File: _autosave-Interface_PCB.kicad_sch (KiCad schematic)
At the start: 40 parts, among them IC1 STM32L412RBT6P, J1 USB_B, J2 AVR-JTAG-10, J3 Conn_01x04, J4 Conn_01x04, J5 Conn_01x04, J6 Conn_01x04, J7 Micro_SD_Card, U1 AMS1117-3.3, Y1 Crystal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

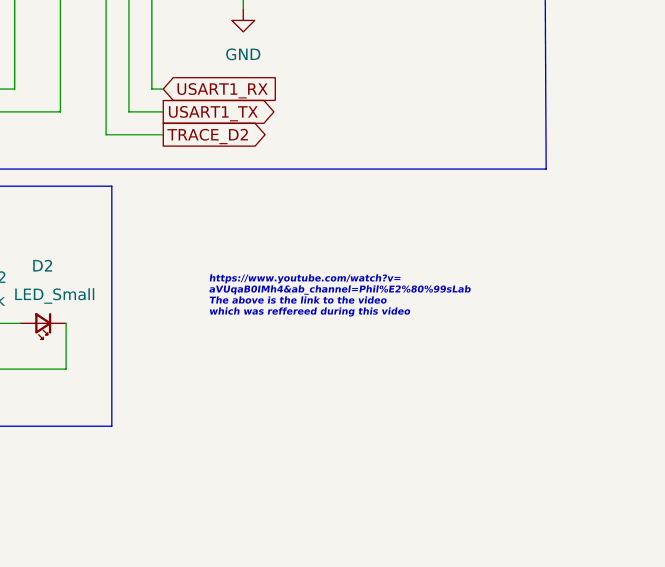
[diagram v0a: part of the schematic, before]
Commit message: README added
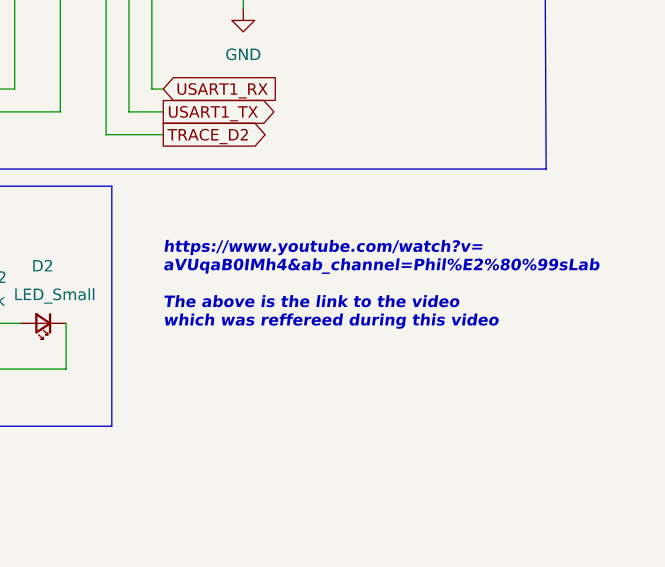
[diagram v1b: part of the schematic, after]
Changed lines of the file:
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@@
     (effects (font (size 0.762 0.762) italic) (justify left bottom))
   )
-  (text "https://www.youtube.com/watch?v=\naVUqaB0IMh4&ab_channel=Phil%E2%80%99sLab\nThe above is the link to the video \nwhich was reffereed during this video "
-    (at 241.3 152.4 0)
-    (effects (font (size 0.762 0.762) (thickness 0.1016) bold italic) (justify left bottom))
+  (text "https://www.youtube.com/watch?v=\naVUqaB0IMh4&ab_channel=Phil%E2%80%99sLab\n\nThe above is the link to the video \nwhich was reffereed during this video "
+    (at 236.22 153.67 0)
+    (effects (font (size 1.27 1.27) (thickness 0.254) bold italic) (justify left bottom))
   )
   (text "Check the connector footprint with \nthe one available in the LAB "
@@
   (symbol (lib_id "power:+3V3") (at 60.96 88.9 0) (unit 1)
     (in_bom yes) (on_board yes) (fields_autoplaced)
-    (property "Reference" "#PWR?" (id 0) (at 60.96 92.71 0)
+    (property "Reference" "#PWR0116" (id 0) (at 60.96 92.71 0)
       (effects (font (size 1.27 1.27)) hide)
     )
@@
   (symbol (lib_id "power:VBUS") (at 17.78 81.28 0) (unit 1)
     (in_bom yes) (on_board yes)
-    (property "Reference" "#PWR?" (id 0) (at 17.78 85.09 0)
+    (property "Reference" "#PWR0117" (id 0) (at 17.78 85.09 0)
       (effects (font (size 1.27 1.27)) hide)
     )
@@
       (reference "#PWR0115") (unit 1) (value "GND") (footprint "")
     )
+    (path "/47eb6540-4ecc-4ac9-ae7f-7bcc7f1af7af"
+      (reference "#PWR0116") (unit 1) (value "+3V3") (footprint "")
+    )
+    (path "/dd7f1cd6-5cbe-4c2a-b90e-3d6470430cf5"
+      (reference "#PWR0117") (unit 1) (value "VBUS") (footprint "")
+    )
     (path "/765b67ce-2c12-4da2-9ba2-0e6a8c2479e2"
       (reference "#PWR0118") (unit 1) (value "GND") (footprint "")
@@
       (reference "#PWR0139") (unit 1) (value "+3.3VA") (footprint "")
     )
-    (path "/47eb6540-4ecc-4ac9-ae7f-7bcc7f1af7af"
-      (reference "#PWR?") (unit 1) (value "+3V3") (footprint "")
-    )
-    (path "/dd7f1cd6-5cbe-4c2a-b90e-3d6470430cf5"
-      (reference "#PWR?") (unit 1) (value "VBUS") (footprint "")
-    )
     (path "/a205f2cb-5dcf-4bfb-8e00-e48b0fecec82"

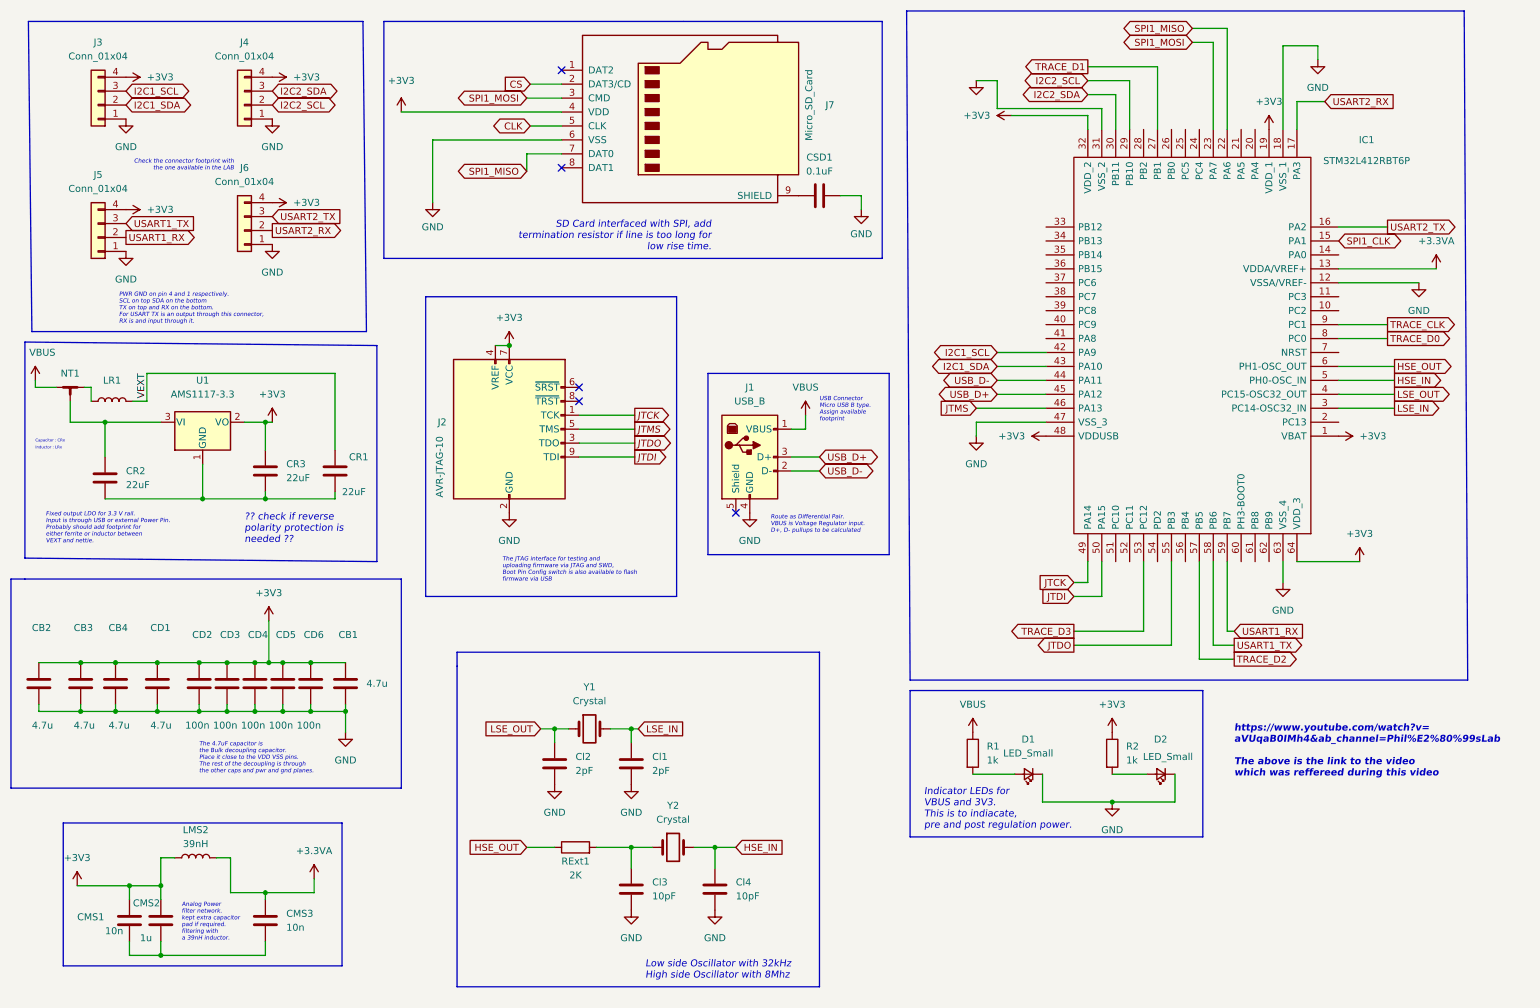
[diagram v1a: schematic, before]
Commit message: Added all component links and modified the footprints
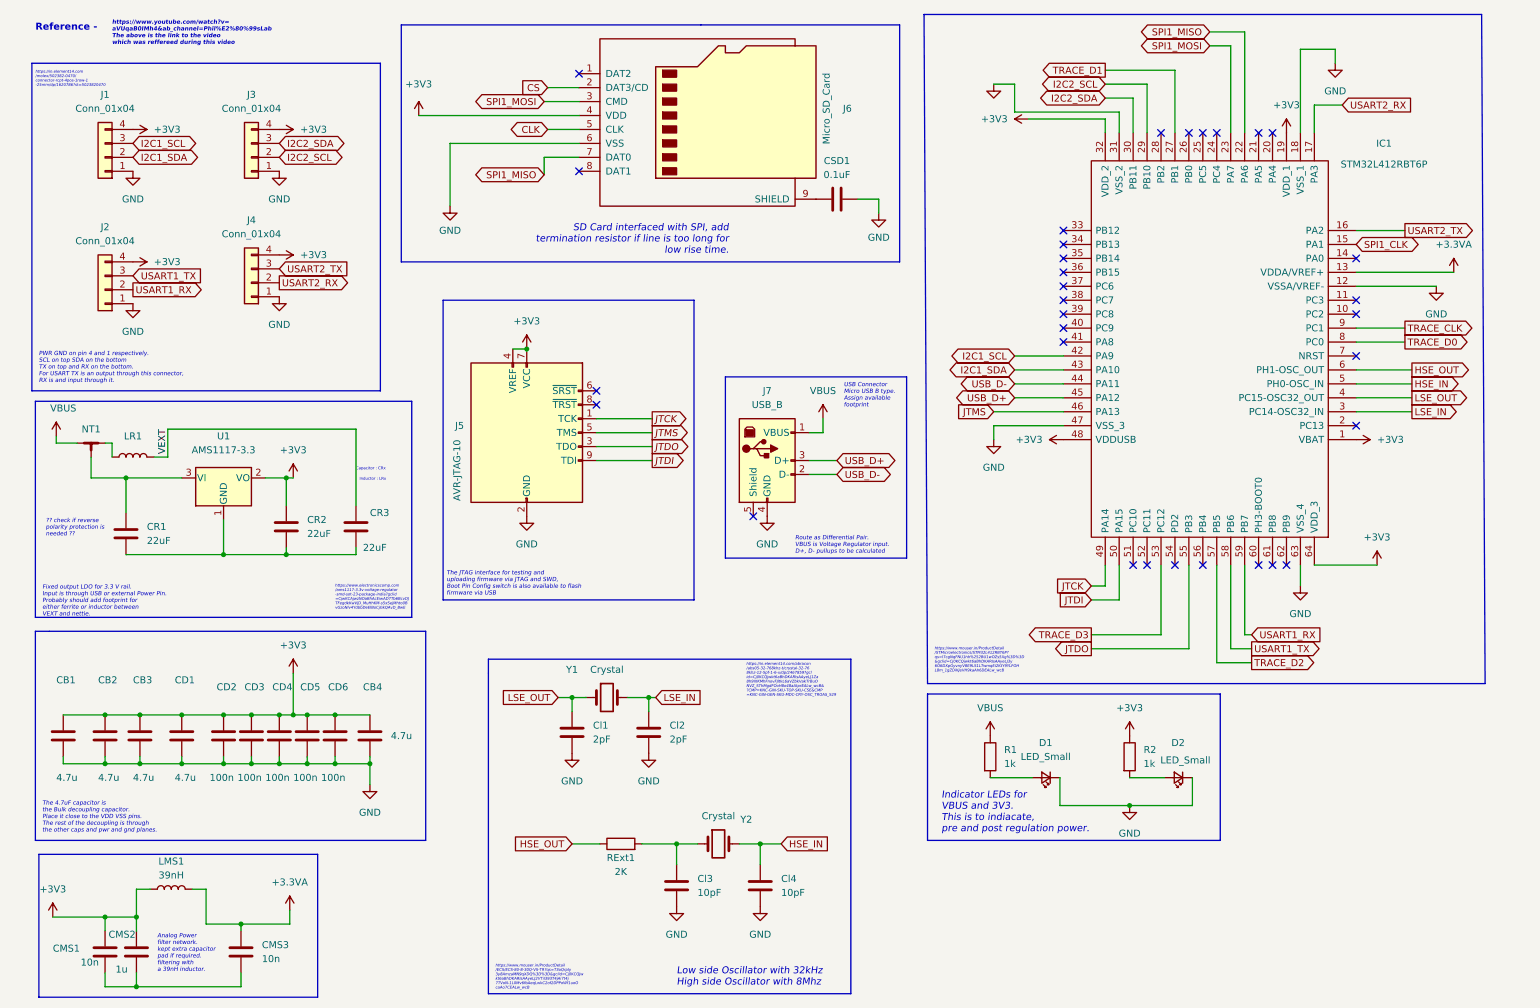
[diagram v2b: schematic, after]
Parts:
- removed J1: USB_B, Connector_USB:USB_Micro-B_Amphenol_10104110_Horizontal, symbol Connector:USB_B
- removed J2: AVR-JTAG-10, Connector_PinHeader_2.54mm:PinHeader_2x05_P2.54mm_Vertical_SMD, symbol Connector:AVR-JTAG-10
- removed J5, J6: Conn_01x04, Connector_Molex:Molex_CLIK-Mate_502382-0470_1x04-1MP_P1.25mm_Vertical, symbol Connector_Generic:Conn_01x04
- removed J7: Micro_SD_Card, Connector_Card:microSD_HC_Wuerth_693072010801, symbol Connector:Micro_SD_Card
- removed LMS2: 39nH, Capacitor_SMD:C_0603_1608Metric, symbol Device:L
- added J1, J2: Conn_01x04, SamacSys_Parts:502382-0470, symbol Connector_Generic:Conn_01x04
- added J5: AVR-JTAG-10, Connector_PinHeader_2.54mm:PinHeader_2x05_P2.54mm_Vertical_SMD, symbol Connector:AVR-JTAG-10
- added J6: Micro_SD_Card, SamacSys_Parts:693072010801, symbol Connector:Micro_SD_Card
- added J7: USB_B, SamacSys_Parts:GMCB05B11124H1EU, symbol Connector:USB_B
- added LMS1: 39nH, Capacitor_SMD:C_0603_1608Metric, symbol Device:L
- CB1, CB2, CB3, CD1: footprint Capacitor_SMD:C_0805_2012Metric -> Capacitor_SMD:C_0402_1005Metric
- CD2, CD3, CD4, CD5, CD6, CMS1, CMS2, CMS3: footprint Capacitor_SMD:C_0603_1608Metric -> Capacitor_SMD:C_0805_2012Metric
- CR1, CR2, CR3, CSD1: footprint (none) -> Capacitor_SMD:C_0402_1005Metric
- D1, D2: footprint LED_SMD:LED_0603_1608Metric -> LED_SMD:LED_0805_2012Metric
- J3, J4: footprint Connector_Molex:Molex_CLIK-Mate_502382-0470_1x04-1MP_P1.25mm_Vertical -> SamacSys_Parts:502382-0470
- LR1: footprint (none) -> Inductor_SMD:L_0402_1005Metric
- NT1: footprint (none) -> NetTie:NetTie-3_SMD_Pad2.0mm
- R1, R2: footprint Resistor_SMD:R_0603_1608Metric -> Resistor_SMD:R_0805_2012Metric
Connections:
- net +3.3VA: now also LMS1.2
- net +3V3: now also CR2.1, J1.4 (Pin_4), J2.4 (Pin_4), J5.4 (VREF), J5.7 (VCC), J6.4 (VDD), LMS1.1; no longer CR3.1
- net CLK: now also J6.5 (CLK)
- net CS: now also J6.2 (DAT3/CD)
- net GND: now also J1.1 (Pin_1), J2.1 (Pin_1), J5.10 (GND), J5.2 (GND), J6.6 (VSS), J7.4 (GND)
- net I2C1_SCL: now also J1.3 (Pin_3); no longer J3.3 (Pin_3)
- net I2C1_SDA: now also J1.2 (Pin_2); no longer J3.2 (Pin_2)
- net I2C2_SCL: now also J3.2 (Pin_2); no longer J4.2 (Pin_2)
- net I2C2_SDA: now also J3.3 (Pin_3); no longer J4.3 (Pin_3)
- net JTCK: now also J5.1 (TCK)
- net JTDI: now also J5.9 (TDI)
- net JTDO: now also J5.3 (TDO)
- net JTMS: now also J5.5 (TMS)
- net LSE_IN: now also Cl2.1; no longer Cl1.1
- net LSE_OUT: now also Cl1.1; no longer Cl2.1
- net SPI1_MISO: now also J6.7 (DAT0)
- net SPI1_MOSI: now also J6.3 (CMD)
- net USART1_RX: now also J2.2 (Pin_2)
- net USART1_TX: now also J2.3 (Pin_3)
- net USART2_RX: now also J4.2 (Pin_2)
- net USART2_TX: now also J4.3 (Pin_3)
- net USB_D+: now also J7.3 (D+)
- net USB_D-: now also J7.2 (D-)
- net VBUS: now also J7.1 (VBUS)
- net VEXT: now also CR3.1; no longer CR1.1
- net at CSD1.1: now also J6.9 (SHIELD)
- net at NT1.3, U1.3 (VI): now also CR1.1; no longer CR2.1
- no-connect marks 5 -> 32
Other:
- note added: "Reference -"
- note added: "https://in.element14.com /molex/502382-0470/ connector-rcpt-4pos-1row-1 -25mm/dp/1620786?st=5023820470"
- note added: "https://in.element14.com/abracon /abs05-32-768khz-t/crystal-32-76 8khz-12-5pf-1-6-x/dp/2467859?gcl id=Cj0KCQjwkt6aBhDKARIsAAyeLJ1Za 8h9IXKMhFnovFJltkL6aVZbkVakTrBuO NVZ_SThMgdFOoH8o48aAtprEALw_wcB& ?CMP=KNC-GIN-SKU-TOP-SKU-CSE&CMP =KNC-GIN-GEN-SKU-MDC-CRY-OSC_TROAS_S29"
- note added: "https://www.electronicscomp.com /ams1117-3.3v-voltage-regulator -smd-sot-23-package-india?gclid =CjwKCAjwzNOaBhAcEiwAD7Tb6BcvDJ TFegdkKwVjD_MuHhKM-s5xSejMhto0B vGzoNlv4YdbbDeElBoCjGkQAvD_BwE"
- note added: "https://www.mouser.in/ProductDetail /ECS/ECS-80-8-30Q-VS-TR?qs=T3oQrply 3y8AmzaMN9qXDQ%3D%3D&gclid=Cj0KCQjw kt6aBhDKARIsAAyeLJ2VTiI393T4jAi7t4j 7TVoN-1L0Mv6fbAeqLwkC2of2DPPoWf1uoO caAo7CEALw_wcB"
- note added: "https://www.mouser.in/ProductDetail /STMicroelectronics/STM32L412RBT6P? qs=l7cgNqFNU1hh%252BU1wOZs5Xg%3D%3D &gclid=Cj0KCQjwkt6aBhDKARIsAAyeLJ3y 6O6DXpGyvnyV8E9LS1LTwmqEi2KtY9YLFOH L8m_1gZDiKJeVH9kaAh6DEALw_wcB"
- note removed: "Check the connector footprint with the one available in the LAB"
